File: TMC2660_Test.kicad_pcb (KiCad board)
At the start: 2 copper layers, 77.7 x 49.9 mm, 70 parts, among them P101 CONN_4, P102 CONN_4, P103 CONN_2, P104 CONN_13X2, P105 CONN_4, P106 CONN_4, P107 CONN_1, P108 CONN_1, P109 CONN_1, P110 CONN_1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

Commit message: Added some notes, labels on silkscreen, and Open Source Hardware logo.
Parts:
- added M101: LOGO_OSHW, oshw_logo_silkscreen-back_40mm, B.Cu at (174.2, 113.9)
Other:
- board text added: "+"
- board text added: "-"
- board text added: "Designed by TopherMan aka Chris George"
- board text added: "E"
- board text added: "GND"
- board text added: "MISO"
- board text added: "MOSI"
- board text added: "SCK"
- board text added: "VCC"
- board text added: "X"
- board text added: "Y"
- board text added: "Z"
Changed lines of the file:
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@@
     (links 246)
     (no_connects 0)
-    (area 134.665 91.634334 213.381 143.9464)
+    (area 135.249999 92.049999 213.050001 142.050001)
     (thickness 1.6)
-    (drawings 5)
+    (drawings 21)
     (tracks 948)
     (zones 0)
-    (modules 70)
+    (modules 71)
     (nets 91)
   )
@@
     )
   )
+  (module oshw_logo_silkscreen-back_40mm (layer B.Cu)
+    (at 174.2 113.9)
+    (fp_text reference M101 (at 0 -21.21662) (layer B.SilkS) hide
+      (effects (font (size 1.82626 1.82626) (thickness 0.36322)) (justify mirror))
+    )
+    (fp_text value LOGO_OSHW (at 0 21.21662) (layer B.SilkS) hide
+      (effects (font (size 1.82626 1.82626) (thickness 0.36322)) (justify mirror))
+    )
+    (fp_poly (pts (xy 12.12596 17.96796) (xy 11.91768 17.85874) (xy 11.44778 17.5641) (xy 10.77976 17.12722)
+      (xy 9.99236 16.5989) (xy 9.19988 16.06296) (xy 8.5471 15.62608) (xy 8.09244 15.33398)
+      (xy 7.90194 15.2273) (xy 7.7978 15.26286) (xy 7.42188 15.44574) (xy 6.87578 15.73022)
+      (xy 6.55828 15.89532) (xy 6.0579 16.11122) (xy 5.80898 16.15694) (xy 5.76834 16.08582)
+      (xy 5.58546 15.70228) (xy 5.2959 15.04696) (xy 4.91744 14.18082) (xy 4.48564 13.16482)
+      (xy 4.02336 12.07008) (xy 3.556 10.95502) (xy 3.11404 9.88822) (xy 2.72542 8.93318)
+      (xy 2.41046 8.1534) (xy 2.20472 7.61238) (xy 2.12852 7.3787) (xy 2.15138 7.33044)
+      (xy 2.40284 7.0866) (xy 2.83972 6.7564) (xy 3.7846 5.98932) (xy 4.71932 4.82346)
+      (xy 5.28828 3.49758) (xy 5.47878 2.02692) (xy 5.31622 0.66294) (xy 4.78028 -0.65786)
+      (xy 3.86588 -1.83642) (xy 2.75844 -2.71272) (xy 1.4605 -3.26644) (xy 0.00508 -3.44678)
+      (xy -1.397 -3.2893) (xy -2.73812 -2.76098) (xy -3.91668 -1.86182) (xy -4.41198 -1.28778)
+      (xy -5.10032 -0.09398) (xy -5.49148 1.1938) (xy -5.53212 1.52146) (xy -5.47624 2.92354)
+      (xy -5.05968 4.26974) (xy -4.318 5.47624) (xy -3.2893 6.46176) (xy -3.15976 6.5532)
+      (xy -2.68224 6.9088) (xy -2.3622 7.15518) (xy -2.11328 7.36092) (xy -3.90144 11.66622)
+      (xy -4.18592 12.35202) (xy -4.67614 13.52804) (xy -5.11048 14.5415) (xy -5.45338 15.34922)
+      (xy -5.69214 15.8877) (xy -5.79882 16.1036) (xy -5.80898 16.1163) (xy -5.96646 16.14424)
+      (xy -6.29666 16.02486) (xy -6.89356 15.73276) (xy -7.29234 15.52956) (xy -7.74954 15.30858)
+      (xy -7.95782 15.2273) (xy -8.128 15.32128) (xy -8.56996 15.6083) (xy -9.21004 16.03502)
+      (xy -9.97966 16.55826) (xy -10.71118 17.0561) (xy -11.38682 17.50314) (xy -11.87958 17.81556)
+      (xy -12.1158 17.9451) (xy -12.1539 17.9451) (xy -12.36726 17.82572) (xy -12.7508 17.50314)
+      (xy -13.34008 16.94942) (xy -14.17066 16.129) (xy -14.29512 16.00454) (xy -14.97838 15.30858)
+      (xy -15.5321 14.72692) (xy -15.90294 14.3129) (xy -16.03756 14.12494) (xy -16.03756 14.1224)
+      (xy -15.91564 13.89126) (xy -15.60576 13.40104) (xy -15.15872 12.71778) (xy -14.61262 11.91768)
+      (xy -13.18768 9.84504) (xy -13.97 7.88924) (xy -14.2113 7.29234) (xy -14.5161 6.5659)
+      (xy -14.74216 6.04774) (xy -14.859 5.82168) (xy -15.07236 5.74548) (xy -15.6083 5.61848)
+      (xy -16.383 5.45592) (xy -17.30756 5.2832) (xy -18.18894 5.12064) (xy -18.9865 4.97332)
+      (xy -19.56054 4.85902) (xy -19.81962 4.80822) (xy -19.88058 4.77266) (xy -19.93392 4.64566)
+      (xy -19.96694 4.37642) (xy -19.98726 3.89128) (xy -19.99742 3.12928) (xy -19.99742 2.02692)
+      (xy -19.99742 1.90754) (xy -19.98726 0.85344) (xy -19.96948 0.01778) (xy -19.939 -0.53848)
+      (xy -19.90344 -0.75438) (xy -19.9009 -0.75692) (xy -19.65198 -0.81788) (xy -19.09064 -0.93726)
+      (xy -18.29562 -1.0922) (xy -17.34312 -1.27254) (xy -17.28724 -1.28524) (xy -16.33982 -1.46558)
+      (xy -15.54734 -1.63068) (xy -14.99362 -1.76022) (xy -14.7574 -1.83134) (xy -14.70914 -1.89992)
+      (xy -14.51864 -2.26822) (xy -14.24686 -2.85496) (xy -13.9319 -3.57124) (xy -13.62456 -4.31546)
+      (xy -13.35786 -4.98094) (xy -13.17752 -5.48132) (xy -13.12418 -5.70738) (xy -13.12672 -5.71246)
+      (xy -13.26896 -5.94106) (xy -13.59408 -6.42874) (xy -14.05382 -7.10946) (xy -14.605 -7.91464)
+      (xy -14.64818 -7.9756) (xy -15.19174 -8.7757) (xy -15.6337 -9.4488) (xy -15.92834 -9.93394)
+      (xy -16.03756 -10.14984) (xy -16.03502 -10.16508) (xy -15.85468 -10.40384) (xy -15.44574 -10.85596)
+      (xy -14.86408 -11.46556) (xy -14.16558 -12.17168) (xy -13.94206 -12.39266) (xy -13.16482 -13.14958)
+      (xy -12.6238 -13.64742) (xy -12.28852 -13.91158) (xy -12.12596 -13.97) (xy -12.12088 -13.96746)
+      (xy -11.87958 -13.82014) (xy -11.37666 -13.49248) (xy -10.68832 -13.02766) (xy -9.87806 -12.47648)
+      (xy -9.82218 -12.43838) (xy -9.02208 -11.89482) (xy -8.3566 -11.44524) (xy -7.88416 -11.13028)
+      (xy -7.67588 -11.00582) (xy -7.64032 -11.00582) (xy -7.3152 -11.0998) (xy -6.74878 -11.30046)
+      (xy -6.04774 -11.57224) (xy -5.3086 -11.86688) (xy -4.63804 -12.15136) (xy -4.13258 -12.3825)
+      (xy -3.89382 -12.51712) (xy -3.88874 -12.52982) (xy -3.80238 -12.8143) (xy -3.66522 -13.4112)
+      (xy -3.49504 -14.2367) (xy -3.30962 -15.2146) (xy -3.27914 -15.37462) (xy -3.0988 -16.32712)
+      (xy -2.9464 -17.11198) (xy -2.83464 -17.65808) (xy -2.77876 -17.8816) (xy -2.64668 -17.91462)
+      (xy -2.17678 -17.94764) (xy -1.46558 -17.96542) (xy -0.60706 -17.97558) (xy 0.30734 -17.96796)
+      (xy 1.18872 -17.95018) (xy 1.94564 -17.92224) (xy 2.48412 -17.88668) (xy 2.71018 -17.84096)
+      (xy 2.7178 -17.82826) (xy 2.80162 -17.53362) (xy 2.93116 -16.93418) (xy 3.10134 -16.1036)
+      (xy 3.2893 -15.12316) (xy 3.32232 -14.95044) (xy 3.50012 -14.00048) (xy 3.66014 -13.2207)
+      (xy 3.77444 -12.68476) (xy 3.8354 -12.47394) (xy 3.92176 -12.42822) (xy 4.31546 -12.25804)
+      (xy 4.95046 -11.99388) (xy 5.7404 -11.67384) (xy 7.57428 -10.93216) (xy 9.81456 -12.4714)
+      (xy 10.02284 -12.6111) (xy 10.83056 -13.15974) (xy 11.4935 -13.6017) (xy 11.95578 -13.89888)
+      (xy 12.14628 -14.0081) (xy 12.16152 -14.00048) (xy 12.38504 -13.8049) (xy 12.82954 -13.38834)
+      (xy 13.4366 -12.79652) (xy 14.14526 -12.09294) (xy 14.66596 -11.5697) (xy 15.28572 -10.93978)
+      (xy 15.67942 -10.5156) (xy 15.89278 -10.24382) (xy 15.96644 -10.08126) (xy 15.94866 -9.9695)
+      (xy 15.80388 -9.7409) (xy 15.47368 -9.24814) (xy 15.0114 -8.56742) (xy 14.4653 -7.7724)
+      (xy 14.01826 -7.10946) (xy 13.52804 -6.35508) (xy 13.21054 -5.8166) (xy 13.10132 -5.55498)
+      (xy 13.12926 -5.44576) (xy 13.2842 -5.00634) (xy 13.55344 -4.34086) (xy 13.89126 -3.55092)
+      (xy 14.67104 -1.77546) (xy 15.8369 -1.5494) (xy 16.54048 -1.41478) (xy 17.526 -1.22682)
+      (xy 18.47342 -1.04394) (xy 19.94916 -0.75692) (xy 19.99996 4.67106) (xy 19.77136 4.76758)
+      (xy 19.55546 4.826) (xy 19.00682 4.94792) (xy 18.22704 5.10286) (xy 17.30756 5.27812)
+      (xy 16.5227 5.4229) (xy 15.73276 5.57276) (xy 15.16634 5.68198) (xy 14.91488 5.73786)
+      (xy 14.84884 5.82168) (xy 14.65072 6.20522) (xy 14.37386 6.81228) (xy 14.0589 7.5438)
+      (xy 13.7414 8.30326) (xy 13.46454 9.00176) (xy 13.26896 9.53516) (xy 13.1953 9.81202)
+      (xy 13.30452 10.0203) (xy 13.6017 10.48512) (xy 14.03858 11.14552) (xy 14.57452 11.93292)
+      (xy 15.113 12.71778) (xy 15.56512 13.38834) (xy 15.88262 13.87094) (xy 16.01216 14.09192)
+      (xy 15.94866 14.24178) (xy 15.6337 14.62024) (xy 15.04188 15.23746) (xy 14.1605 16.10868)
+      (xy 14.01826 16.24838) (xy 13.31468 16.92148) (xy 12.72286 17.46504) (xy 12.30884 17.83588)
+      (xy 12.12596 17.96796)) (layer B.SilkS) (width 0.00254))
+  )
+  (gr_text "Designed by TopherMan aka Chris George" (at 211.7 117.9 90) (layer B.SilkS)
+    (effects (font (size 1 1) (thickness 0.2)) (justify mirror))
+  )
+  (gr_text SCK (at 170.4 114.2) (layer F.SilkS)
+    (effects (font (size 0.5 0.5) (thickness 0.1)))
+  )
+  (gr_text MOSI (at 170.5 109.1) (layer F.SilkS)
+    (effects (font (size 0.5 0.5) (thickness 0.1)))
+  )
+  (gr_text MISO (at 170.5 111.6) (layer F.SilkS)
+    (effects (font (size 0.5 0.5) (thickness 0.1)))
+  )
+  (gr_text Z (at 177.7 101.3) (layer F.SilkS)
+    (effects (font (size 1.5 1.5) (thickness 0.3)))
+  )
+  (gr_text X (at 170.7 101.4) (layer F.SilkS)
+    (effects (font (size 1.5 1.5) (thickness 0.3)))
+  )
+  (gr_text Y (at 170.7 122.8) (layer F.SilkS)
+    (effects (font (size 1.5 1.5) (thickness 0.3)))
+  )
+  (gr_text E (at 177.6 122.8) (layer F.SilkS)
+    (effects (font (size 1.5 1.5) (thickness 0.3)))
+  )
+  (gr_text - (at 176.5 132.9) (layer F.SilkS)
+    (effects (font (size 1.5 1.5) (thickness 0.3)))
+  )
+  (gr_text + (at 171.4 132.9) (layer F.SilkS)
+    (effects (font (size 1.5 1.5) (thickness 0.3)))
+  )
+  (gr_text GND (at 174.2 129.5) (layer F.SilkS)
+    (effects (font (size 1.5 1.5) (thickness 0.3)))
+  )
+  (gr_text VCC (at 174.2 93.7) (layer F.SilkS)
+    (effects (font (size 1.5 1.5) (thickness 0.3)))
+  )
+  (gr_text "E\n" (at 209.9 123.5 90) (layer F.SilkS)
+    (effects (font (size 1.5 1.5) (thickness 0.3)))
+  )
+  (gr_text Z (at 210 111.7 90) (layer F.SilkS)
+    (effects (font (size 1.5 1.5) (thickness 0.3)))
+  )
+  (gr_text Y (at 138.5 123.1 270) (layer F.SilkS)
+    (effects (font (size 1.5 1.5) (thickness 0.3)))
+  )
+  (gr_text X (at 138.7 112.4 90) (layer F.SilkS)
+    (effects (font (size 1.5 1.5) (thickness 0.3)))
+  )
   (gr_line (start 213 141.9) (end 213 142) (angle 90) (layer Edge.Cuts) (width 0.1))

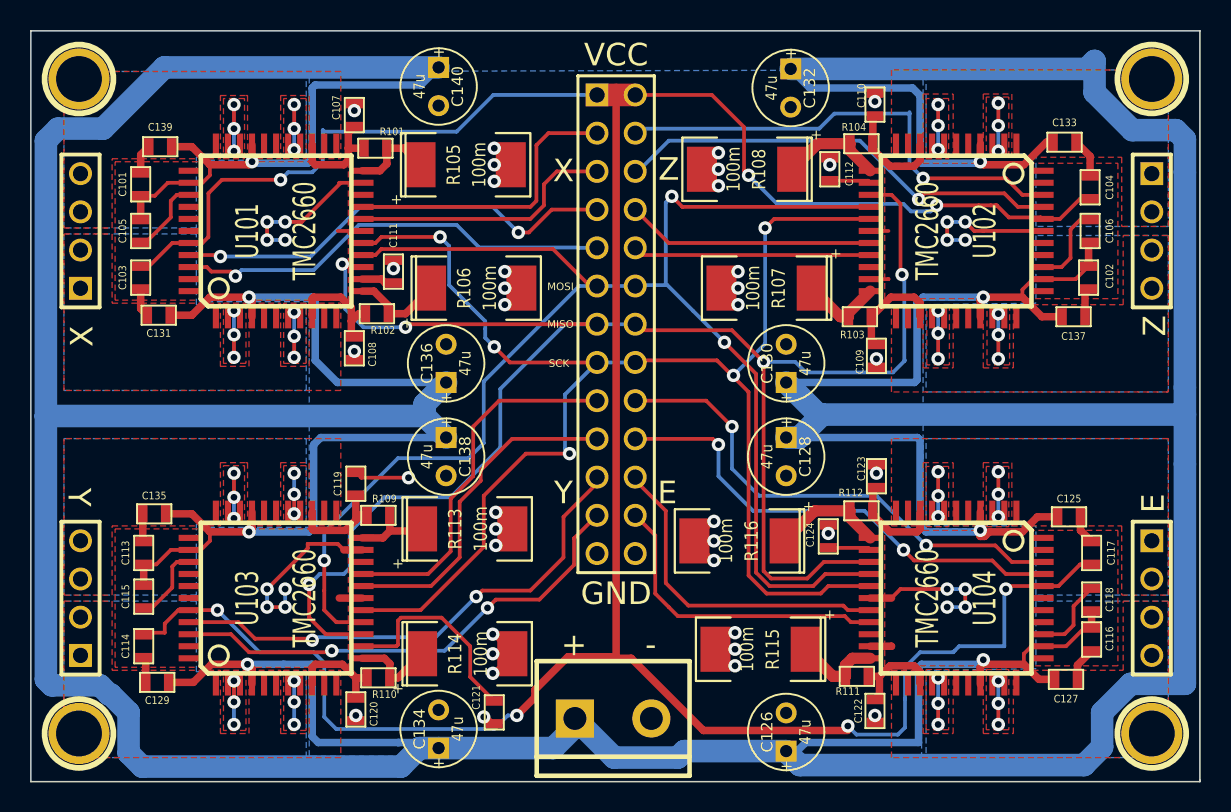
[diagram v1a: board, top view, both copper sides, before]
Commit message: Begin fixing tracks, and fix stupid fill errors.
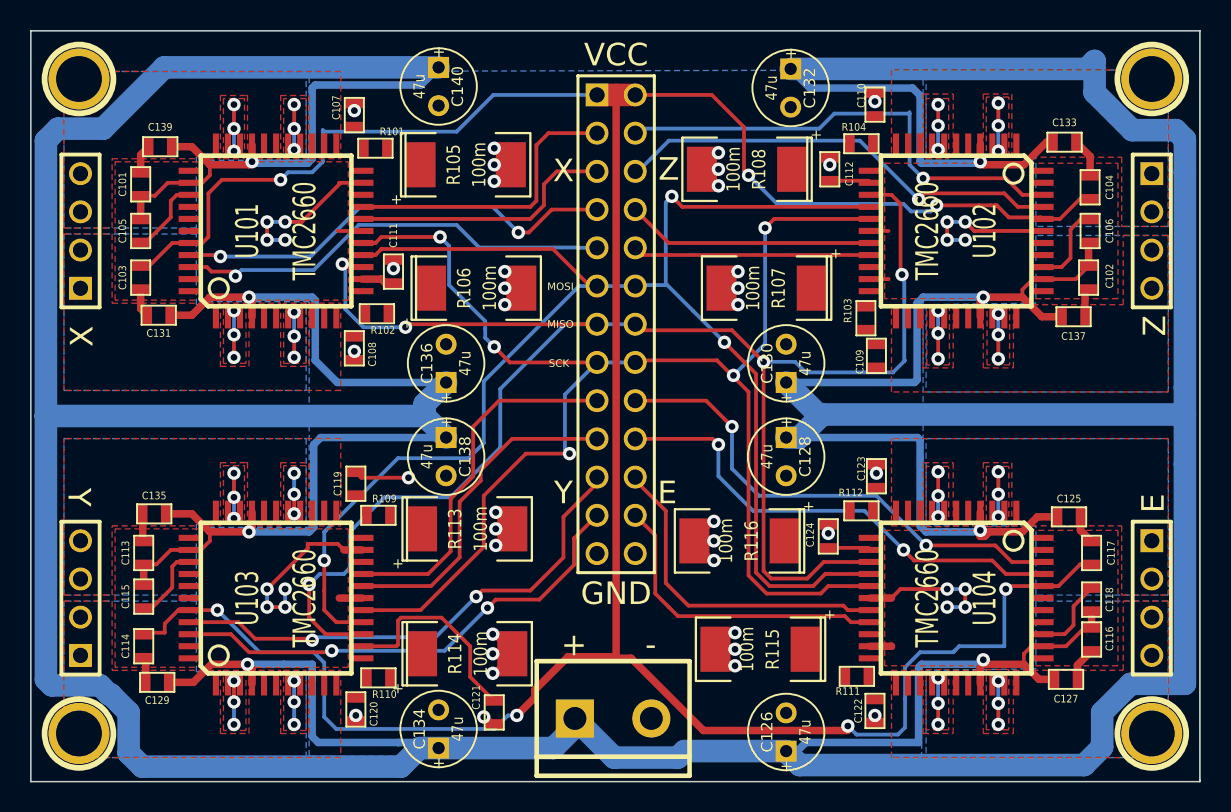
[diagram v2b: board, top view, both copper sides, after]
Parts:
- R101, R102, R103, R104, R109, R110, R111, R112: value 200 -> 22
- moved R103 0.41 mm to (190.8, 111.2), turned to 270 degrees
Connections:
- C107 pad 1: N-0000054 -> N-0000053
- C108 pad 1: N-0000052 -> N-0000055
- C109 pad 1: N-0000086 -> N-0000088
- C119 pad 1: N-0000022 (its old number) -> N-0000023
- C120 pad 1: N-0000023 -> N-0000021
- C122 pad 1: N-0000049 -> N-0000018
- C123 pad 1: N-0000046 (its old number) -> N-0000016
- R102 pad 2: N-0000056 (its old number) -> N-0000055
- R103 pad 2: N-0000086 -> N-0000085
- R104 pad 1: N-0000087 -> N-0000086
- R104 pad 2: N-0000085 -> N-0000087
- R105 pad 1: N-0000053 -> N-0000054
- R106 pad 1: N-0000056 (its old number) -> N-0000052
- R107 pad 1: N-0000088 -> N-0000085
- R108 pad 1: N-0000085 -> N-0000086
- R109 pad 1: N-0000019 -> N-0000023
- R109 pad 2: N-0000022 (its old number) -> N-0000024
- R110 pad 1: N-0000023 -> N-0000025
- R111 pad 1: N-0000047 -> N-0000018
- R111 pad 2: N-0000049 -> N-0000047
- R112 pad 1: N-0000046 (its old number) -> N-0000048
- R112 pad 2: N-0000048 -> N-0000016
- R113 pad 1: N-0000019 -> N-0000024
- R114 pad 1: N-0000021 -> N-0000025
- U101 pad 12: N-0000056 (its old number) -> N-0000055
- U102 pad 12: N-0000085 -> N-0000087
- U102 pad 25: N-0000086 -> N-0000085
- U102 pad 9: N-0000087 -> N-0000086
- U103 pad 22: N-0000019 -> N-0000023
- U103 pad 25: N-0000022 (its old number) -> N-0000024
- U103 pad 9: N-0000023 -> N-0000025
- U104 pad 12: N-0000048 -> N-0000016
- U104 pad 22: N-0000047 -> N-0000018
- U104 pad 25: N-0000049 -> N-0000047
- U104 pad 9: N-0000046 (its old number) -> N-0000048
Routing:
- net N-0000048: track 7.52 -> 0.00 mm
- net N-0000052: track 7.31 -> 0.00 mm
- net N-0000054: track 7.16 -> 0.00 mm
- net N-0000087: track 7.05 -> 0.00 mm
- net N-0000085: track 6.90 -> 0.00 mm
- net N-0000022 (its old number): track 6.85 -> 0.00 mm
- net N-0000086: track 6.84 -> 0.00 mm
- net N-0000046 (its old number): track 6.71 -> 0.00 mm
- net N-0000023: track 6.55 -> 0.00 mm
- net N-0000049: track 6.37 -> 0.00 mm
- net N-0000056 (its old number): track 6.23 -> 0.00 mm
- net N-0000047: track 5.96 -> 0.00 mm
- net N-0000021: track 5.74 -> 0.00 mm
- net N-0000053: track 5.57 -> 0.00 mm
- net N-0000088: track 5.52 -> 0.00 mm
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
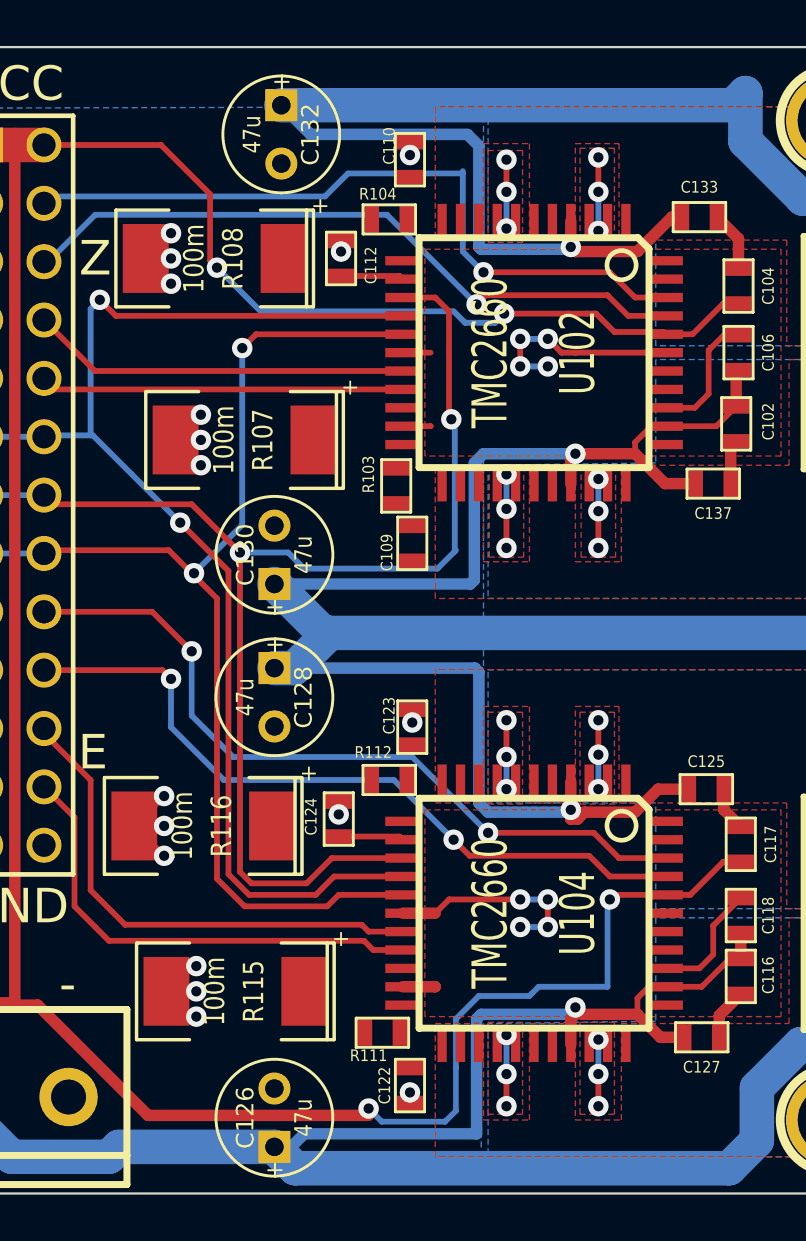
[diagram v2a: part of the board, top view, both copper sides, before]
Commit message: Tracks half fixed. Considering dumping input protection.
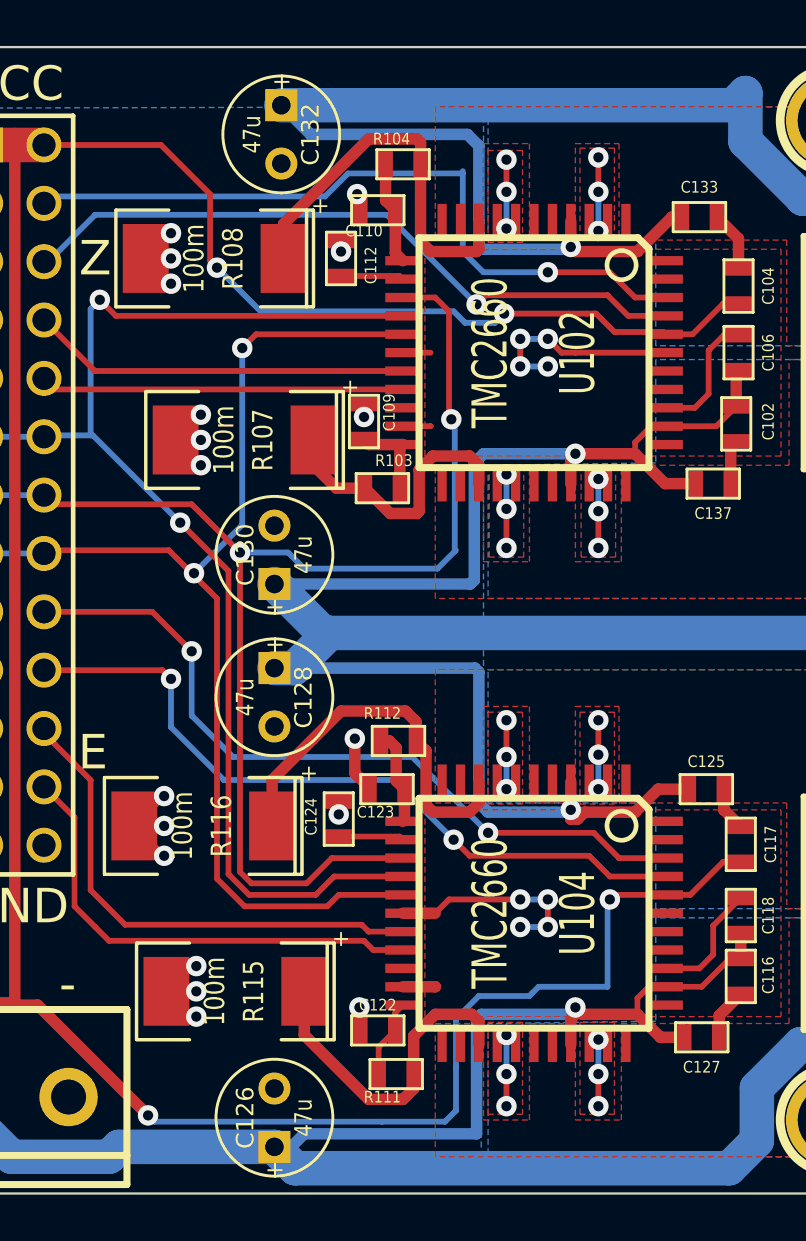
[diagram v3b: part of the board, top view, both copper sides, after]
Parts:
- moved C109 5.70 mm to (189.4, 108.4), turned to 90 degrees
- moved C123 2.92 mm to (190.4, 124.4), turned to 180 degrees
- moved C122 2.78 mm to (190.0, 134.9), turned to 180 degrees
- moved C110 2.61 mm to (190.0, 99.2), turned to 180 degrees
- moved R104 2.47 mm to (191.1, 97.2)
- moved R111 1.90 mm to (190.8, 136.8)
- moved R112 1.75 mm to (190.9, 122.3)
- moved R103 0.61 mm to (190.2, 111.3), turned to 180 degrees
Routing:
- net N-0000086: track 0.00 -> 17.3 mm
- net N-0000048: track 0.00 -> 17.0 mm
- net N-0000047: track 0.00 -> 14.7 mm
- net N-0000085: track 0.00 -> 12.2 mm
- net N-0000087: track 0.00 -> 4.51 mm
- net N-0000016: track 0.00 -> 4.17 mm
- net N-0000088: track 0.00 -> 3.76 mm
- net N-0000018: track 0.00 -> 3.43 mm
- net GND: track 108.8 -> 112.1 mm, vias 51 -> 52
